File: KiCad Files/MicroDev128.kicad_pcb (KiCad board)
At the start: 4 copper layers, 49.1 x 17.8 mm, 27 parts, among them J1 UPDI Header, J3 GPIO, J4 PWR and ANALOG, SW1 SW_SP3T, SW2 RST, U1 AVR128DB32x-xRXB, U2 LT8653SEV_PBF, Y1 24MHz

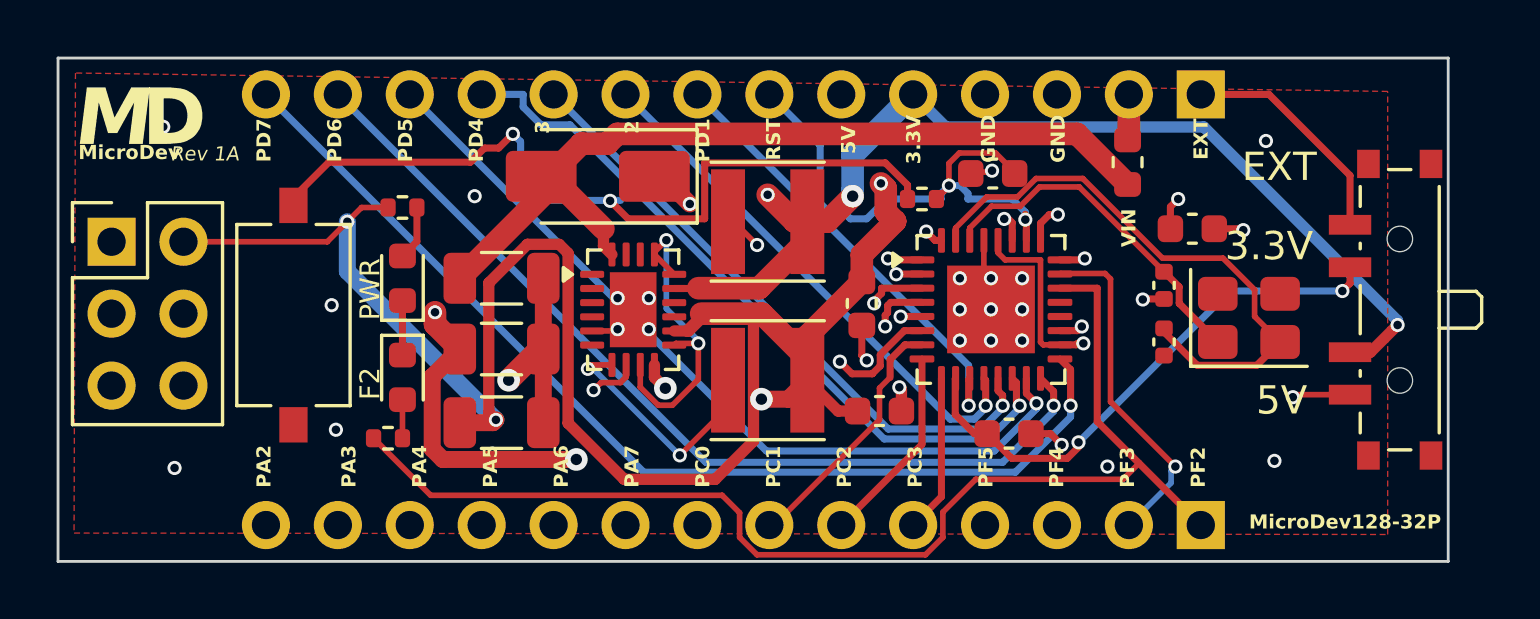
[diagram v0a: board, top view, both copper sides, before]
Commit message: Update to clarift Costs and fix errors
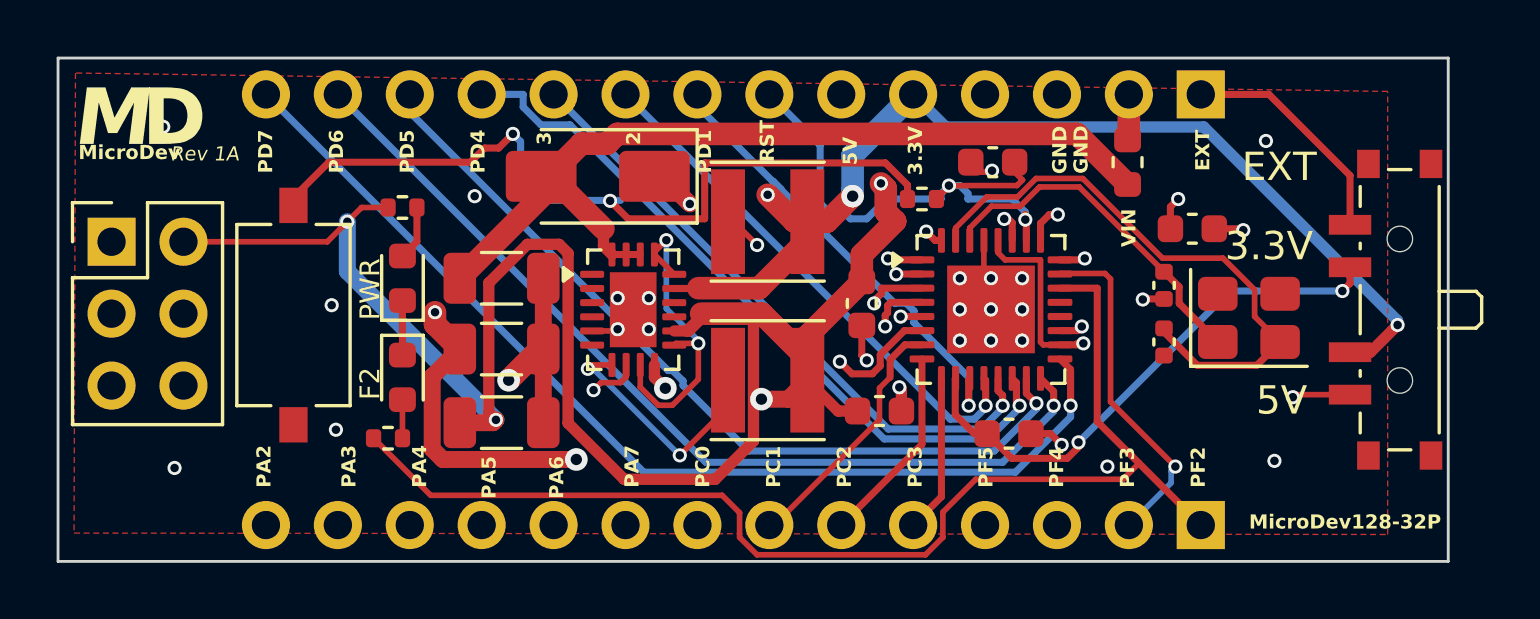
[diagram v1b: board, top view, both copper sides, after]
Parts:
- moved C10 0.40 mm to (103.5, 56.5)
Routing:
- net Net-(D3-A2): track 30.3 -> 31.3 mm
- net Net-(J4-Pin_12): track 29.2 -> 29.9 mm

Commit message: Updated for sponsor
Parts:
- removed C11, C12: 12pF, Capacitor_SMD:C_0402_1005Metric
- removed Y1: 24MHz, Crystal:Crystal_SMD_3225-4Pin_3.2x2.5mm
- added G***: LOGO, LOGO, B.Cu at (95.5, 62.1)
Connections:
- R3 pad 1: Net-(J3-Pin_1) -> Net-(U1-XTAL32K2/PF1)
- U1 pad 21: unconnected-(U1-XTAL32K2/PF1-Pad21) -> Net-(U1-XTAL32K2/PF1)
- U1 pad 30: Net-(U1-XTALHF1/PA0) -> unconnected-(U1-XTALHF1/PA0-Pad30)
- U1 pad 31: Net-(U1-XTALHF2/PA1) -> unconnected-(U1-XTALHF2/PA1-Pad31)
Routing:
- net Net-(U1-XTAL32K2/PF1): track 0.00 -> 36.0 mm, vias 0 -> 4
- net Net-(J3-Pin_1): track 42.3 -> 11.0 mm
- net Net-(U1-XTALHF2/PA1): track 20.6 -> 0.00 mm
- net Net-(U1-XTALHF1/PA0): track 12.4 -> 0.00 mm
- net GND: track 22.7 -> 21.9 mm, vias 30 -> 29
